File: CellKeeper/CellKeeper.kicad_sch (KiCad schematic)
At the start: 487 parts, among them J1 Screw_Terminal_01x04, J10 3.81P Screw Terminal, J11 USB_C_Receptacle_USB2.0_16P, J12 Conn_02x10_Odd_Even, J13 USB_C_Receptacle_USB2.0_16P, J14 ZE05H-8DP-2H, J15 Screw_Terminal_01x04, J16 Conn_01x03, J17 OEM HV Sense Connector, J18 7.62mm Pitch Screw Terminal, J19 USB_C_Receptacle_USB2.0_16P, J2 Screw_Terminal_01x01, J20 OEM Connector, J21 3.81P Screw Terminal, J22 Conn_02x10_Odd_Even, J3 Screw_Terminal_01x04, J4 8P8C_LED_Shielded_x2, J5 8P8C_LED_Shielded_x2, J6 S44B-RAD1AK, J7 Screw_Terminal_01x04, J8 Conn_01x03, J9 USB_C_Receptacle_USB2.0_16P, K5 Link Positive, K6 Link Negative, K7 FC Negative, K8 FC Positive, Q1 BSC0805LS, Q2 BSC0805LS, Q3 BSC0805LS, Q4 BSC0805LS, SW1 TS-1187A-B-A-B, SW2 TS-1187A-B-A-B, SW3 TS-1187A-B-A-B, SW4 TS-1187A-B-A-B, U1 UCC27524DR, U10 ISO1050DUB, U11 UCC27524DR, U12 LTV-217-B-G, U13 LTV-217-B-G, U14 RP2354B, U15 F0505S-1WR3, U16 ISO1540, U17 INA228, U18 ADS1115, U19 ADS1115, U20 RP2354B, U21 SP3485EN-L/TR, U22 AM26LV32EIDR, U25 TLV1117LV33DCYR, U26 TLV1117LV33DCYR, U3 TPS5430DDAR, U4 F0505S-1WR3, U5 ISO1050DUB, U6 LTV-217-B-G, U7 LTV-217-B-G, U8 LTV-217-B-G, U9 LTV-217-B-G, Y1 ABM8-272-T3, Y2 ABM8-272-T3

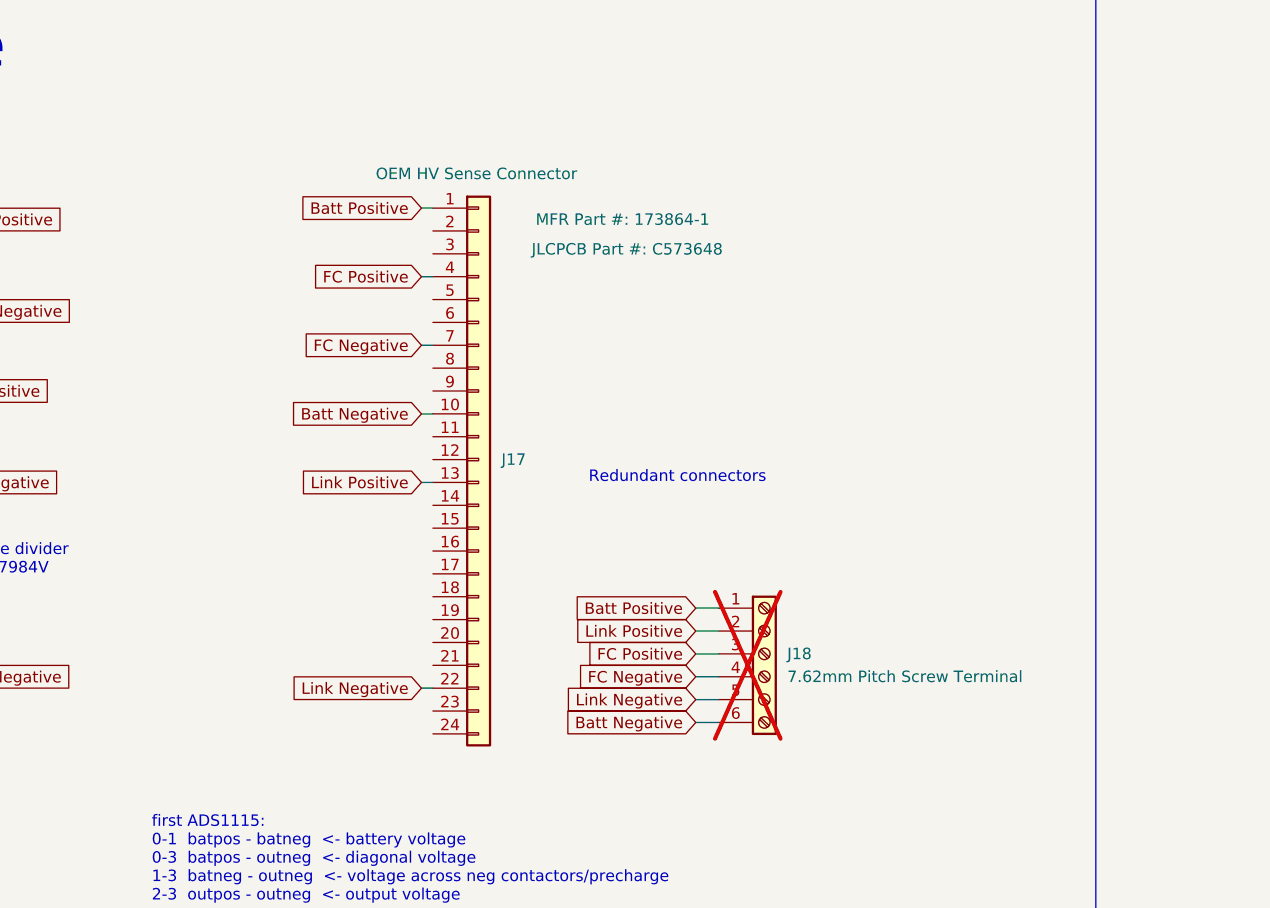
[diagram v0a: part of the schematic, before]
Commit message: Update Symbol HV Sense
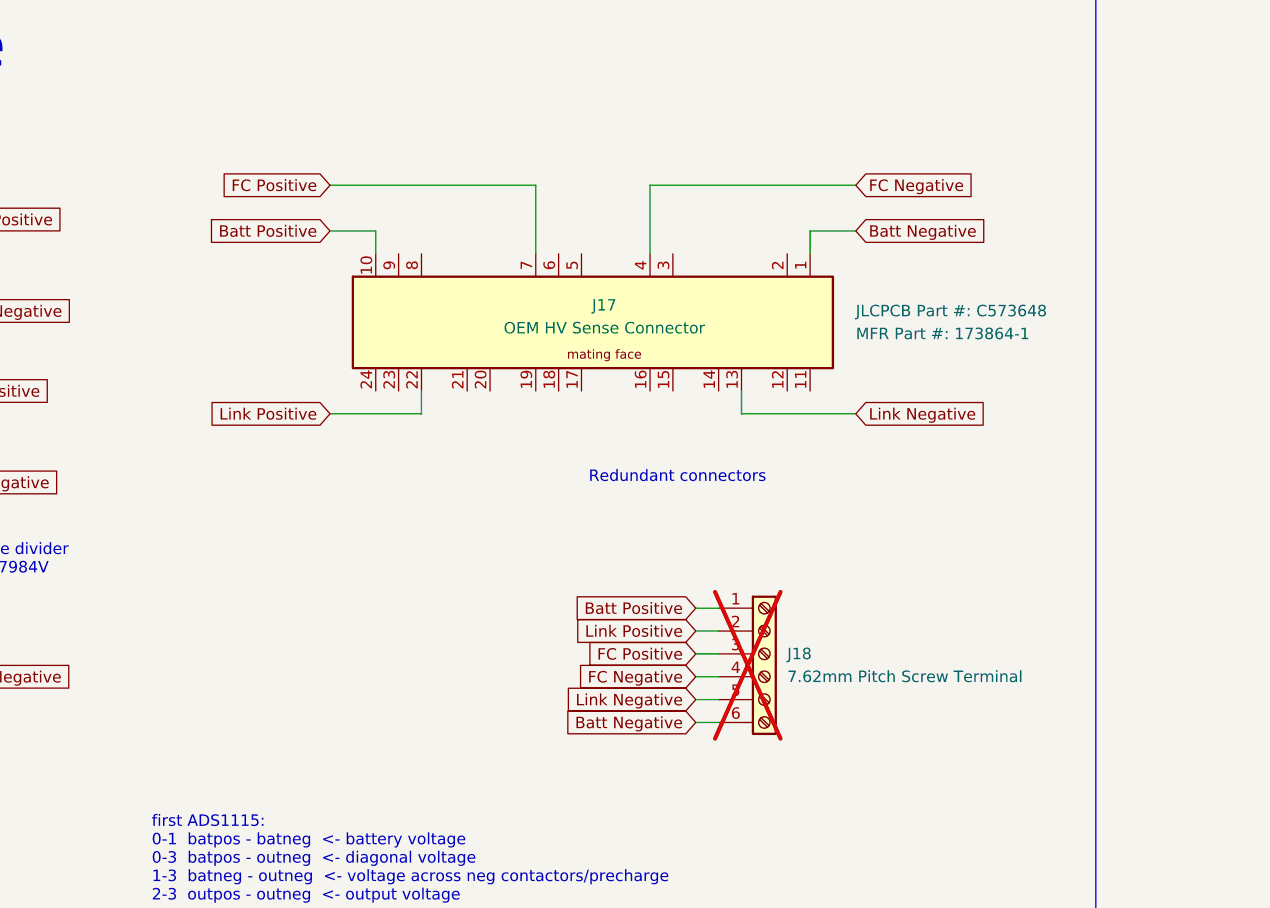
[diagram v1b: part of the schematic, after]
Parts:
- J17: symbol CellKeeper_Local:Connector_Generic__Conn_01x24 -> CellKeeper_Local:Connector__TE_173864-1
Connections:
- net Batt Negative: now also J17.1; no longer J17.10 (Pin_10)
- net Batt Positive: now also J17.10; no longer J17.1 (Pin_1)
- net FC Negative: now also J17.4; no longer J17.7 (Pin_7)
- net FC Positive: now also J17.7; no longer J17.4 (Pin_4)
- net Link Negative: now also J17.13; no longer J17.22 (Pin_22)
- net Link Positive: now also J17.22; no longer J17.13 (Pin_13)
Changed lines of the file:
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@@
 	(wire
 		(pts
+			(xy 466.09 393.7) (xy 466.09 391.16)
+		)
+		(stroke
+			(width 0)
+			(type default)
+		)
+	)
+	(wire
+		(pts
+			(xy 466.09 391.16) (xy 461.01 391.16)
+		)
+		(stroke
+			(width 0)
+			(type default)
+		)
+	)
+	(wire
+		(pts
+			(xy 483.87 393.7) (xy 483.87 386.08)
+		)
+		(stroke
+			(width 0)
+			(type default)
+		)
+	)
+	(wire
+		(pts
+			(xy 483.87 386.08) (xy 461.01 386.08)
+		)
+		(stroke
+			(width 0)
+			(type default)
+		)
+	)
+	(wire
+		(pts
+			(xy 496.57 393.7) (xy 496.57 386.08)
+		)
+		(stroke
+			(width 0)
+			(type default)
+		)
+	)
+	(wire
+		(pts
+			(xy 496.57 386.08) (xy 519.43 386.08)
+		)
+		(stroke
+			(width 0)
+			(type default)
+		)
+	)
+	(wire
+		(pts
+			(xy 514.35 393.7) (xy 514.35 391.16)
+		)
+		(stroke
+			(width 0)
+			(type default)
+		)
+	)
+	(wire
+		(pts
+			(xy 514.35 391.16) (xy 519.43 391.16)
+		)
+		(stroke
+			(width 0)
+			(type default)
+		)
+	)
+	(wire
+		(pts
+			(xy 471.17 408.94) (xy 471.17 411.48)
+		)
+		(stroke
+			(width 0)
+			(type default)
+		)
+	)
+	(wire
+		(pts
+			(xy 471.17 411.48) (xy 461.01 411.48)
+		)
+		(stroke
+			(width 0)
+			(type default)
+		)
+	)
+	(wire
+		(pts
+			(xy 506.73 408.94) (xy 506.73 411.48)
+		)
+		(stroke
+			(width 0)
+			(type default)
+		)
+	)
+	(wire
+		(pts
+			(xy 506.73 411.48) (xy 519.43 411.48)
+		)
+		(stroke
+			(width 0)
+			(type default)
+		)
+	)
+	(wire
+		(pts
 			(xy 184.15 228.6) (xy 184.15 231.14)
 		)
@@
 	(wire
 		(pts
-			(xy 471.17 419.1) (xy 472.44 419.1)
-		)
-		(stroke
-			(width 0)
-			(type default)
-		)
-	)
-	(wire
-		(pts
 			(xy 100.33 322.58) (xy 102.87 322.58)
 		)
@@
 	(wire
 		(pts
-			(xy 471.17 403.86) (xy 472.44 403.86)
-		)
-		(stroke
-			(width 0)
-			(type default)
-		)
-	)
-	(wire
-		(pts
 			(xy 152.4 594.36) (xy 152.4 589.28)
 		)
@@
 	(wire
 		(pts
-			(xy 471.17 388.62) (xy 472.44 388.62)
-		)
-		(stroke
-			(width 0)
-			(type default)
-		)
-	)
-	(wire
-		(pts
 			(xy 933.45 111.76) (xy 933.45 114.3)
 		)
@@
 	(wire
 		(pts
-			(xy 471.17 396.24) (xy 472.44 396.24)
-		)
-		(stroke
-			(width 0)
-			(type default)
-		)
-	)
-	(wire
-		(pts
 			(xy 920.75 383.54) (xy 920.75 377.19)
 		)
@@
 	(wire
 		(pts
-			(xy 471.17 411.48) (xy 472.44 411.48)
-		)
-		(stroke
-			(width 0)
-			(type default)
-		)
-	)
-	(wire
-		(pts
 			(xy 501.65 445.77) (xy 504.19 445.77)
 		)
@@
 	(wire
 		(pts
-			(xy 471.17 441.96) (xy 472.44 441.96)
-		)
-		(stroke
-			(width 0)
-			(type default)
-		)
-	)
-	(wire
-		(pts
 			(xy 713.74 109.22) (xy 713.74 93.98)
 		)
@@
 	(global_label "Link Positive"
 		(shape input)
-		(at 471.17 419.1 180)
+		(at 461.01 411.48 180)
 		(fields_autoplaced yes)
 		(effects
@@
 		)
 		(property "Intersheetrefs" "${INTERSHEET_REFS}"
-			(at 455.9686 419.1 0)
+			(at 445.8086 411.48 0)
 			(hide yes)
 			(show_name no)
@@
 	(global_label "Batt Positive"
 		(shape input)
-		(at 471.17 388.62 180)
+		(at 461.01 391.16 180)
 		(fields_autoplaced yes)
 		(effects
@@
 		)
 		(property "Intersheetrefs" "${INTERSHEET_REFS}"
-			(at 455.9082 388.62 0)
+			(at 445.7482 391.16 0)
 			(hide yes)
 			(show_name no)
@@
 	(global_label "Link Negative"
 		(shape input)
-		(at 471.17 441.96 180)
+		(at 519.43 411.48 0)
 		(fields_autoplaced yes)
 		(effects
@@
 				(size 1.27 1.27)
 			)
-			(justify right)
+			(justify left)
 		)
 		(property "Intersheetrefs" "${INTERSHEET_REFS}"
-			(at 455.3034 441.96 0)
+			(at 535.2966 411.48 0)
 			(hide yes)
 			(show_name no)
@@
 					(size 1.27 1.27)
 				)
-				(justify right)
+				(justify left)
 			)
 		)
@@
 	(global_label "FC Negative"
 		(shape input)
-		(at 471.17 403.86 180)
+		(at 519.43 386.08 0)
 		(fields_autoplaced yes)
 		(effects
@@
 				(size 1.27 1.27)
 			)
-			(justify right)
+			(justify left)
 		)
 		(property "Intersheetrefs" "${INTERSHEET_REFS}"
-			(at 456.7548 403.86 0)
+			(at 533.8452 386.08 0)
 			(hide yes)
 			(show_name no)
@@
 					(size 1.27 1.27)
 				)
-				(justify right)
+				(justify left)
 			)
 		)
@@
 	(global_label "FC Positive"
 		(shape input)
-		(at 471.17 396.24 180)
+		(at 461.01 386.08 180)
 		(fields_autoplaced yes)
 		(effects
@@
 		)
 		(property "Intersheetrefs" "${INTERSHEET_REFS}"
-			(at 457.42 396.24 0)
+			(at 447.26 386.08 0)
 			(hide yes)
 			(show_name no)
@@
 	(global_label "Batt Negative"
 		(shape input)
-		(at 471.17 411.48 180)
+		(at 519.43 391.16 0)
 		(fields_autoplaced yes)
 		(effects
@@
 				(size 1.27 1.27)
 			)
-			(justify right)
+			(justify left)
 		)
 		(property "Intersheetrefs" "${INTERSHEET_REFS}"
-			(at 455.243 411.48 0)
+			(at 535.357 391.16 0)
 			(hide yes)
 			(show_name no)
@@
 					(size 1.27 1.27)
 				)
-				(justify right)
+				(justify left)
 			)
 		)
@@
 	)
 	(symbol
-		(lib_id "CellKeeper_Local:Connector_Generic__Conn_01x24")
-		(at 477.52 416.56 0)
+		(lib_id "CellKeeper_Local:Connector__TE_173864-1")
+		(at 491.49 401.32 0)
 		(unit 1)
 		(body_style 1)
@@
 		(dnp no)
 		(property "Reference" "J17"
-			(at 480.06 416.5599 0)
+			(at 491.49 399.415 0)
 			(show_name no)
 			(do_not_autoplace no)
@@
 					(size 1.27 1.27)
 				)
-				(justify left)
 			)
 		)
 		(property "Value" "OEM HV Sense Connector"
-			(at 466.09 384.81 0)
+			(at 491.49 401.955 0)
 			(show_name no)
 			(do_not_autoplace no)
@@
 					(size 1.27 1.27)
 				)
-				(justify left)
 			)
 		)
 		(property "Footprint" "CellKeeper_Local:BMS_Library__CONN_173864-1_TYC_Empty_Pins"
-			(at 477.52 416.56 0)
+			(at 491.49 401.32 0)
 			(hide yes)
 			(show_name no)
@@
 		)
 		(property "Datasheet" ""
-			(at 477.52 416.56 0)
+			(at 491.49 401.32 0)
 			(hide yes)
 			(show_name no)
@@
 			)
 		)
-		(property "Description" "Generic connector, single row, 01x24, script generated (kicad-library-utils/schlib/autogen/connector/)"
-			(at 477.52 416.56 0)
+		(property "Description" "TE 070 Multilock 24-position right-angle PCB header, TE circuit numbering, pins drawn as on the PCB"
+			(at 491.49 401.32 0)
 			(hide yes)
 			(show_name no)
@@
 		)
 		(property "JLCPCB Part #" "C573648"
-			(at 494.03 393.192 0)
+			(at 519.43 400.05 0)
 			(show_name yes)
 			(do_not_autoplace no)
@@
 					(size 1.27 1.27)
 				)
+				(justify left)
 			)
 		)
 		(property "MFR Part #" "173864-1"
-			(at 493.522 389.89 0)
+			(at 519.43 402.59 0)
 			(show_name yes)
 			(do_not_autoplace no)
@@
 					(size 1.27 1.27)
 				)
+				(justify left)
 			)
 		)

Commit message: Add 3D-printable enclosure for the main board (build123d)
enclosure/cellkeeper_case.py builds a base tray and lid around the board:
- M3 screws from below self-tap into the lid pillars at H1/H2/H7/H8 (and
  H3/H4 while BOARD_SCREWS_AT_H3_H4 is set); 45 deg screw seats print
  without support
- flat lid top 20 mm above the PCB with 4.3 mm bracket holes over H3/H4
  for the penthouse mounting brackets
- connector openings, J6 passing through the lid, ground-screw slot,
  button guide tubes and LED light tunnels
- lid markings as true curves: the silkscreen logo refit as lines and
  splines, KiBuzzard-style labels built from the KiBuzzard font
- print files as STEP/STL (whole and split for 256 mm beds), with
  separate inlay and light-pipe parts for multi-colour printing
- an interference check against the board's STEP export

Also:
- CellKeeper_Enclosure board-only footprint (ENC1 at 0,0) showing the
  case models in KiCad's 3D viewer
- recolor_vendor_step_models.py colours J20's terminals and hold-downs
  metal on the fused vendor solid
- board and schematic: current working changes, including the H7/H8
  mounting holes, the D34 move and the ENC1 enclosure footprint
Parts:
- removed J13: USB_C_Receptacle_USB2.0_16P, symbol CellKeeper_Local:Connector__USB_C_Receptacle_USB2.0_16P
- added H7, H8: MountingHole_Pad, CellKeeper_Local:MountingHole__MountingHole_3.7mm, symbol CellKeeper_Local:Mechanical__MountingHole_Pad
- J1, J15: value Screw_Terminal_01x04 -> WJ15EDGRC-3.81-04P-14-00A
- J2: value Screw_Terminal_01x01 -> T34008
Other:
- note added: "13V-16V input"
- note added: "Matching connector: WJ15EDGK-3.81-04P-14-00A"
- note removed: "10V-16V input"

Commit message: Rev 1.1 as ordered from JLCPCB on 2026-10-28
- RP2350 symbol: one library symbol for the RP2350B or RP2354B, used by
  U14 and U20 with the same nets as before
- W25Q16JV flash (U23, U24) on each MCU's QSPI bus, marked DNP: the
  RP2354B's in-package flash already sits on that bus and chip select
- H0505S-1WR2 courtyard extended 0.6 mm (U4, U15)
- Back silkscreen moved back into place with the rest of the board; hole
  in the E-STOP DISABLE label around JP37; fonts embedded
- Production files for REV1.1; REV1 BOM, CPL and designators moved into
  production/CellKeeper_REV1 beside its Gerbers
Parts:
- removed JP1, JP2: 0r, CellKeeper_Local:BMS_Library__J_0603_jumper, symbol CellKeeper_Local:BMS_Library__Jumper_Resistor
- added C105, C57: 100n, CellKeeper_Local:Capacitor_SMD__C_0402_1005Metric, symbol CellKeeper_Local:Device__C
- added JP38, JP39: jumper-bridged, CellKeeper_Local:Jumper__SolderJumper-2_P1.3mm_Bridged_RoundedPad1.0x1.5mm, symbol CellKeeper_Local:Jumper__SolderJumper_2_Bridged
- added R86: 510r, CellKeeper_Local:Resistor_SMD__R_0603_1608Metric, symbol CellKeeper_Local:Device__R_Small
- added TP45: TestPoint_2Pole, CellKeeper_Local:BMS_Library__TestPoint_2Pads_Pitch2.54mm_Pad1.5_Drill1.0mm, symbol CellKeeper_Local:Connector__TestPoint_2Pole
- added U23, U24: W25Q16JVUXIQ, Package_SON:Winbond_USON-8-1EP_3x2mm_P0.5mm_EP0.2x1.6mm, symbol Memory_Flash:W25Q16JVSS
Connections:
- net +3.3V: now also C105.1, C57.1, U23.8 (VCC), U24.8 (VCC)
- net C FC-Pos (GND): now also JP38.2 (B), JP39.2 (B)
- net Drive Unit Pos: no longer F4.1
- net FC Pos: no longer F4.2
- net FC-Pos-Jumper: now also JP38.1 (A), JP39.1 (A)
- net GND: now also C105.2, C57.2, U23.4 (GND), U24.4 (GND)
- net GND_Shunt: now also R86.2
- net Shunt Sense +: now also TP45.2
- net Shunt Sense -: now also TP45.1
- net Shunt_5V: now also R86.1
- net QSPI2_SCLK: no longer names the net of U20.71 (QSPI_SCLK)
- net QSPI2_SCLK: now also U24.6 (CLK)
- net QSPI2_SD0: no longer names the net of U20.72 (QSPI_SD0)
- net QSPI2_SD0: now also U24.5 (DI/IO_{0})
- net QSPI2_SD1: no longer names the net of U20.74 (QSPI_SD1)
- net QSPI2_SD1: now also U24.2 (DO/IO_{1})
- net QSPI2_SD2: no longer names the net of U20.73 (QSPI_SD2)
- net QSPI2_SD2: now also U24.3 (~{WP}/IO_{2})
- net QSPI2_SD3: no longer names the net of U20.70 (QSPI_SD3)
- net QSPI2_SD3: now also U24.7 (~{HOLD}/~{RESET}/IO_{3})
- net QSPI2_SS: no longer names the net of R94.1, U20.75 (QSPI_SS)
- net QSPI2_SS: now also U24.1 (~{CS})
- net QSPI_SCLK: no longer names the net of U14.71 (QSPI_SCLK)
- net QSPI_SCLK: now also U23.6 (CLK)
- net QSPI_SD0: no longer names the net of U14.72 (QSPI_SD0)
- net QSPI_SD0: now also U23.5 (DI/IO_{0})
- net QSPI_SD1: no longer names the net of U14.74 (QSPI_SD1)
- net QSPI_SD1: now also U23.2 (DO/IO_{1})
- net QSPI_SD2: no longer names the net of U14.73 (QSPI_SD2)
- net QSPI_SD2: now also U23.3 (~{WP}/IO_{2})
- net QSPI_SD3: no longer names the net of U14.70 (QSPI_SD3)
- net QSPI_SD3: now also U23.7 (~{HOLD}/~{RESET}/IO_{3})
- net QSPI_SS: no longer names the net of R55.1, U14.75 (QSPI_SS)
- net QSPI_SS: now also U23.1 (~{CS})
- net RUN_2: no longer names the net of R95.1, U20.35 (RUN)
- net SWCLK_2: no longer names the net of J16.1 (Pin_1), U20.33 (SWCLK)
- net SWD_2: no longer names the net of J16.3 (Pin_3), U20.34 (SWD)
- net XIN: no longer names the net of C39.1, U14.30 (XIN), Y1.1
- net XIN_2: no longer names the net of C70.1, U20.30 (XIN), Y2.1
- net XOUT: no longer names the net of R53.1, U14.31 (XOUT)
- net XOUT_2: no longer names the net of R92.1, U20.31 (XOUT)
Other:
- note added: "Alternate Part Numbers C468683 (ADS1115IDGST)"
- note added: "Alternative INA237AIDGSR C2864837 - less resolution - pin compatible"
- note added: "Inductor Alternate Parts (untested) APS201610M3R3F C48783272 MHT201610SG-3R3M H C49435043"
- note removed: "FC positive contactor not used (no 12V connection)"
- note removed: "jumper wire from existing 63A PCS or heat pump fuse"
- moved on the sheet: BT5, BT6, BT7, BT8, C39, C40, C70, C71, Cell1, Cell2, Cell3, F3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
